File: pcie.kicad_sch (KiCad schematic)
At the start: 21 parts, among them U15 XC7K160T-FFG676

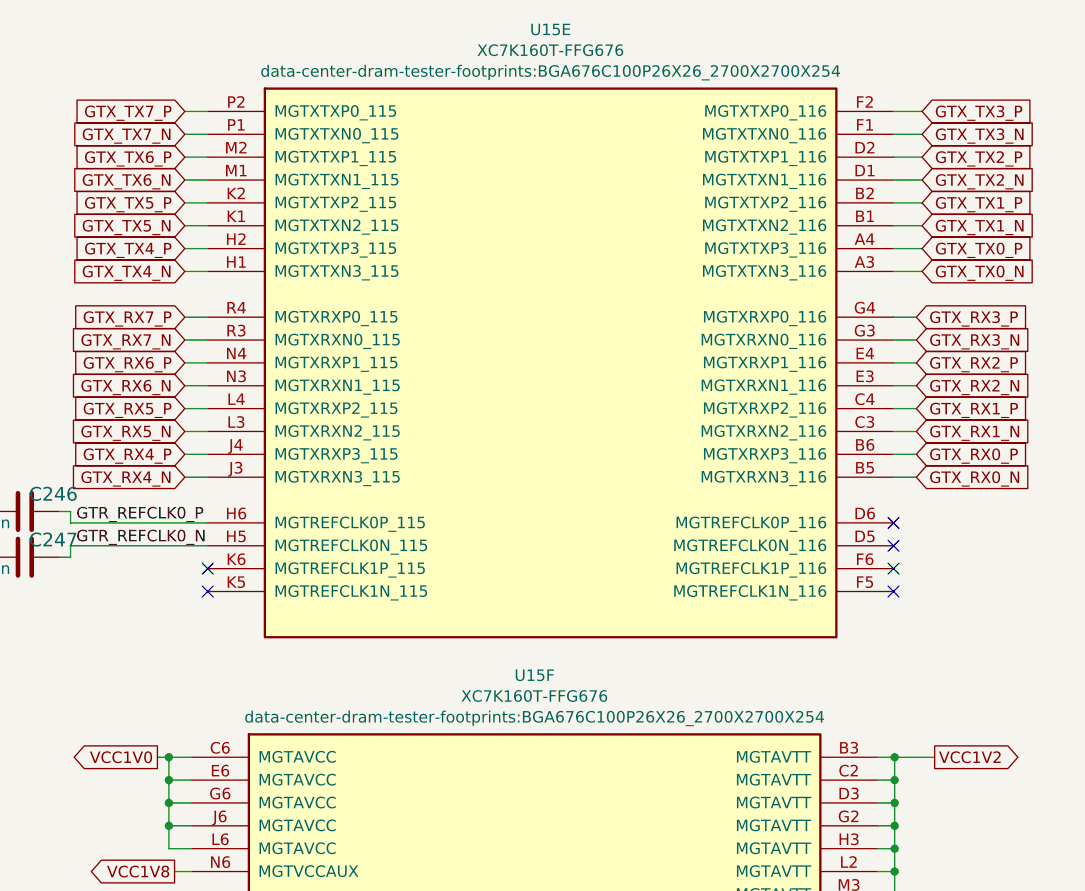
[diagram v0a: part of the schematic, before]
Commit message: Update FPGA symbol (die to pad length), initial fanout for die [1..4]
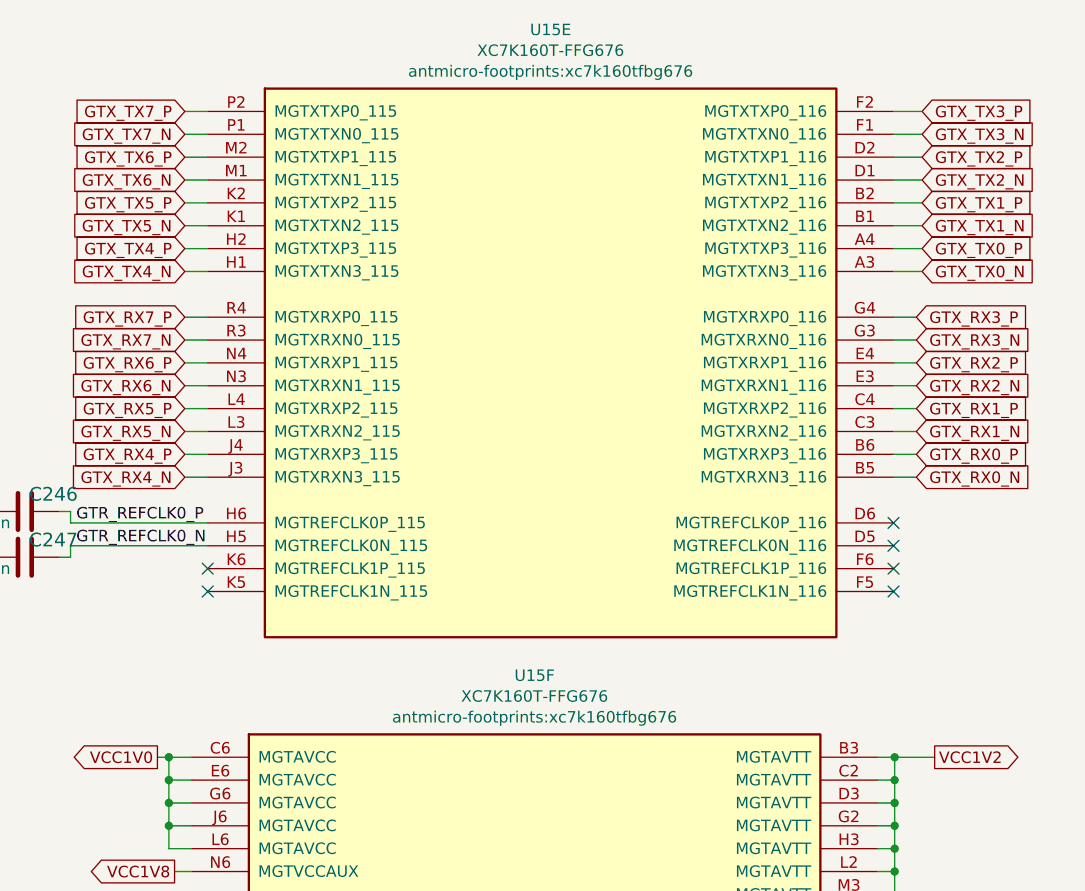
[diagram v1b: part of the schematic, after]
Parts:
- U15: footprint data-center-dram-tester-footprints:BGA676C100P26X26_2700X2700X254 -> antmicro-footprints:xc7k160tfbg676
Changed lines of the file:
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@@
     (property "Reference" "U15" (id 0) (at 155.067 105.8672 0))
     (property "Value" "XC7K160T-FFG676" (id 1) (at 155.067 108.1786 0))
-    (property "Footprint" "data-center-dram-tester-footprints:BGA676C100P26X26_2700X2700X254" (id 2) (at 155.067 110.49 0))
+    (property "Footprint" "antmicro-footprints:xc7k160tfbg676" (id 2) (at 155.067 110.49 0))
     (property "Datasheet" "" (id 3) (at 155.067 127.635 0))
     (pin "AA21")
@@
     (property "Reference" "U15" (id 0) (at 156.845 34.1122 0))
     (property "Value" "XC7K160T-FFG676" (id 1) (at 156.845 36.4236 0))
-    (property "Footprint" "data-center-dram-tester-footprints:BGA676C100P26X26_2700X2700X254" (id 2) (at 156.845 38.735 0))
+    (property "Footprint" "antmicro-footprints:xc7k160tfbg676" (id 2) (at 156.845 38.735 0))
     (property "Datasheet" "" (id 3) (at 156.845 71.12 0))
     (pin "AA21")

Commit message: Cleanup schematic
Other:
- note added: "BANK 115"
- note added: "BANK 116"
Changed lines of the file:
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@@
   (title_block
     (title "Data Center DRAM Tester")
-    (date "2022-09-07")
+    (date "2022-10-31")
     (rev "1.2.0")
     (comment 1 "www.antmicro.com")
@@
   )
   (junction (at 136.525 172.974) (diameter 0) (color 0 0 0 0)
-  )
-  (junction (at 62.992 184.15) (diameter 0) (color 0 0 0 0)
   )
   (junction (at 82.042 184.15) (diameter 0) (color 0 0 0 0)
@@
     (stroke (width 0) (type default) (color 0 0 0 0))
   )
-  (wire (pts (xy 56.515 184.15) (xy 62.992 184.15))
-    (stroke (width 0) (type default) (color 0 0 0 0))
-  )
   (wire (pts (xy 194.945 81.28) (xy 197.485 81.28))
     (stroke (width 0) (type default) (color 0 0 0 0))
@@
     (stroke (width 0) (type default) (color 0 0 0 0))
   )
+  (text "BANK 115" (at 104.14 34.29 0)
+    (effects (font (size 2.4892 2.4892) (thickness 0.4978) bold) (justify left bottom))
+  )
+  (text "BANK 116" (at 189.23 34.29 0)
+    (effects (font (size 2.4892 2.4892) (thickness 0.4978) bold) (justify left bottom))
+  )
   (text "Trace length from the resistor pins to the\nFPGA pins MGTRREF and MGTAVTTRCAL\nmust be equal in length."

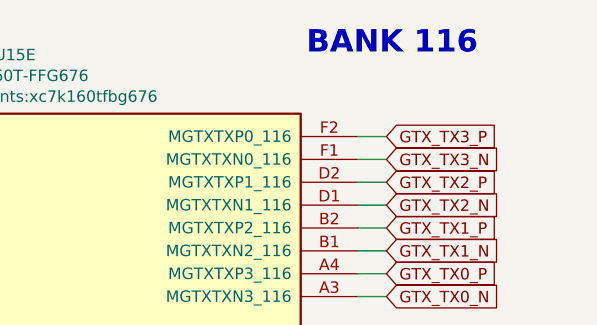
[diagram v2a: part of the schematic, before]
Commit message: Replace visualisation in README and schematic
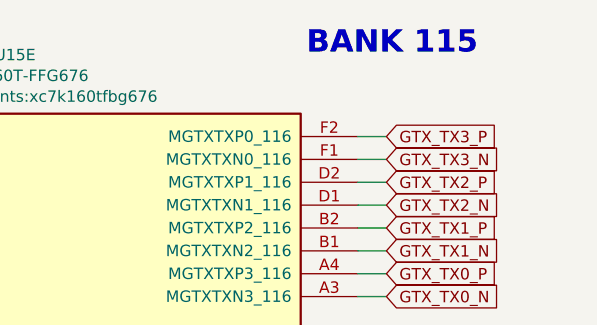
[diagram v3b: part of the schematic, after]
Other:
- note removed: "BANK 116"
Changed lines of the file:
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@@
     (effects (font (size 2.4892 2.4892) (thickness 0.4978) bold) (justify left bottom))
   )
-  (text "BANK 116" (at 189.23 34.29 0)
+  (text "BANK 115" (at 189.23 34.29 0)
     (effects (font (size 2.4892 2.4892) (thickness 0.4978) bold) (justify left bottom))
   )

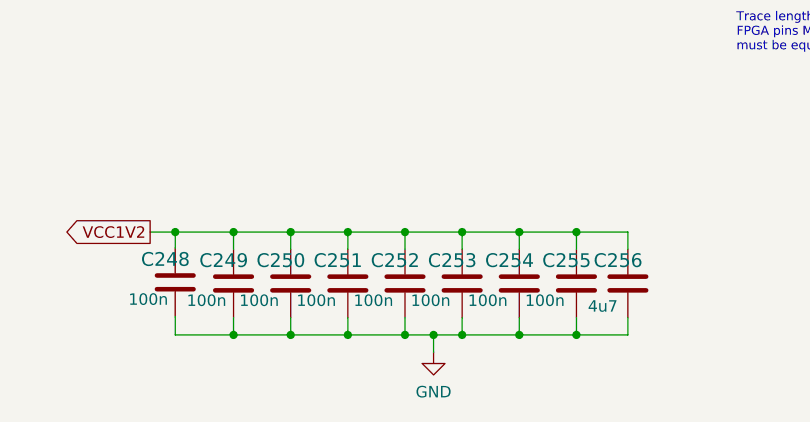
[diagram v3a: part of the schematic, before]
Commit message: Assign and connect misc. signals. Add, place and route decoupling capacitors
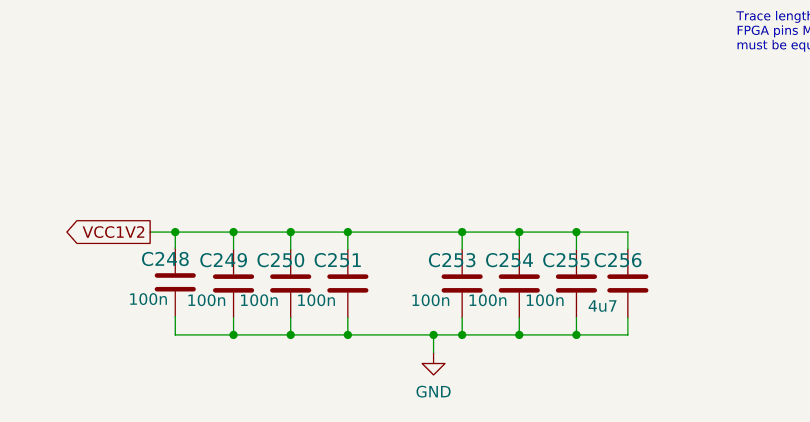
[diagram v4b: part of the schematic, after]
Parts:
- removed C252: C_100n_0201, antmicro-footprints:0201-res, symbol antmicroCapacitorsmisc:C_100n_0201
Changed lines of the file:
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@@
   (junction (at 146.05 184.404) (diameter 0) (color 0 0 0 0)
   )
-  (junction (at 142.875 184.404) (diameter 0) (color 0 0 0 0)
-  )
   (junction (at 130.175 172.974) (diameter 0) (color 0 0 0 0)
   )
@@
   )
   (junction (at 195.072 114.935) (diameter 0) (color 0 0 0 0)
-  )
-  (junction (at 142.875 172.974) (diameter 0) (color 0 0 0 0)
   )
   (junction (at 75.692 184.15) (diameter 0) (color 0 0 0 0)
@@
     (stroke (width 0) (type default) (color 0 0 0 0))
   )
-  (wire (pts (xy 142.875 172.974) (xy 149.225 172.974))
+  (wire (pts (xy 136.525 172.974) (xy 149.225 172.974))
     (stroke (width 0) (type default) (color 0 0 0 0))
   )
@@
     (stroke (width 0) (type default) (color 0 0 0 0))
   )
-  (wire (pts (xy 142.875 184.404) (xy 136.525 184.404))
+  (wire (pts (xy 136.525 184.404) (xy 146.05 184.404))
     (stroke (width 0) (type default) (color 0 0 0 0))
   )
@@
     (stroke (width 0) (type default) (color 0 0 0 0))
   )
-  (wire (pts (xy 136.525 172.974) (xy 142.875 172.974))
-    (stroke (width 0) (type default) (color 0 0 0 0))
-  )
   (wire (pts (xy 87.63 88.9) (xy 90.17 88.9))
     (stroke (width 0) (type default) (color 0 0 0 0))
@@
     (stroke (width 0) (type default) (color 0 0 0 0))
   )
-  (wire (pts (xy 142.875 184.404) (xy 146.05 184.404))
-    (stroke (width 0) (type default) (color 0 0 0 0))
-  )
   (wire (pts (xy 62.992 172.72) (xy 62.992 174.625))
     (stroke (width 0) (type default) (color 0 0 0 0))
@@
     (stroke (width 0) (type default) (color 0 0 0 0))
   )
-  (wire (pts (xy 142.875 182.499) (xy 142.875 184.404))
-    (stroke (width 0) (type default) (color 0 0 0 0))
-  )
   (wire (pts (xy 116.205 76.2) (xy 118.745 76.2))
     (stroke (width 0) (type default) (color 0 0 0 0))
@@
   )
   (wire (pts (xy 116.205 45.72) (xy 118.745 45.72))
-    (stroke (width 0) (type default) (color 0 0 0 0))
-  )
-  (wire (pts (xy 142.875 172.974) (xy 142.875 174.879))
     (stroke (width 0) (type default) (color 0 0 0 0))
   )
@@
     (pin "1")
     (pin "2")
-  )
-  (symbol (lib_id "antmicroCapacitorsmisc:C_100n_0201") (at 142.875 178.689 0) (unit 1)
-    (in_bom yes) (on_board yes)
-    (property "Reference" "C252" (id 0) (at 139.065 176.149 0)
-      (effects (font (size 1.524 1.524)) (justify left))
-    )
-    (property "Value" "C_100n_0201" (id 1) (at 142.875 182.499 0)
-      (effects (font (size 1.524 1.524)) hide)
-    )
-    (property "Footprint" "antmicro-footprints:0201-res" (id 2) (at 147.955 173.609 0)
-      (effects (font (size 1.524 1.524)) (justify left) hide)
-    )
-    (property "Datasheet" "" (id 3) (at 142.875 178.689 0)
-      (effects (font (size 1.27 1.27)) hide)
-    )
-    (property "Manufacturer" "YAGEO" (id 4) (at 147.955 168.529 0)
-      (effects (font (size 1.524 1.524)) (justify left) hide)
-    )
-    (property "MPN" "CC0201KRX6S5BB104" (id 5) (at 147.955 171.069 0)
-      (effects (font (size 1.524 1.524)) (justify left) hide)
-    )
-    (property "Val" "100n" (id 6) (at 137.16 180.594 0)
-      (effects (font (size 1.27 1.27)) (justify left))
-    )
-    (pin "1")
-    (pin "2")

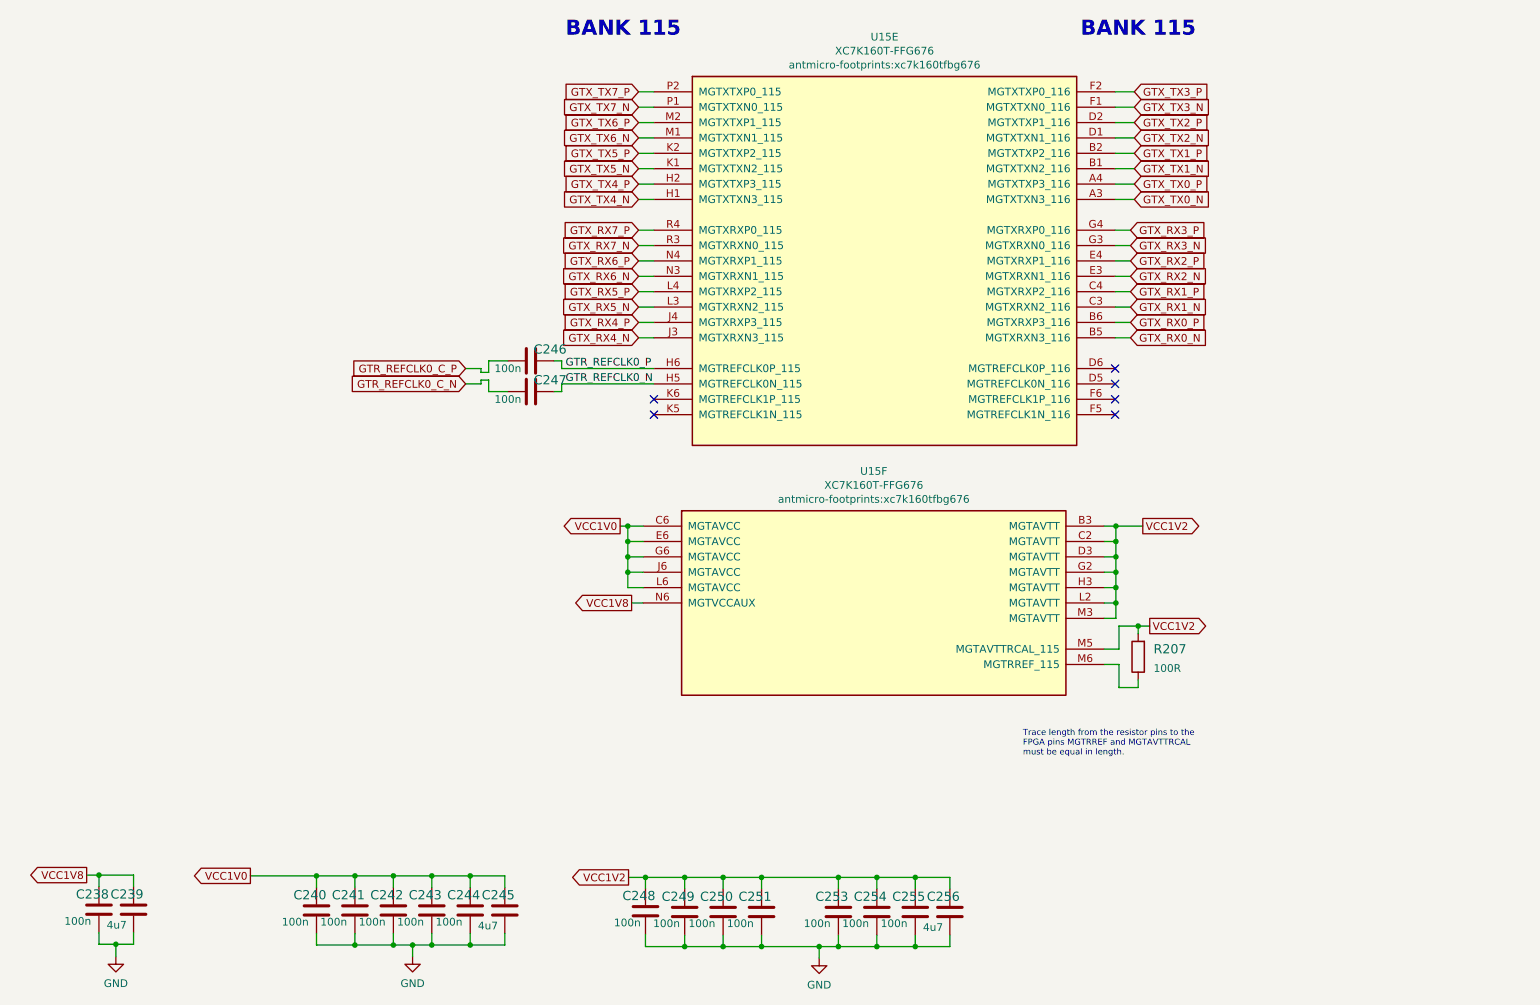
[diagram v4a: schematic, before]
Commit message: Draw power supply polygons
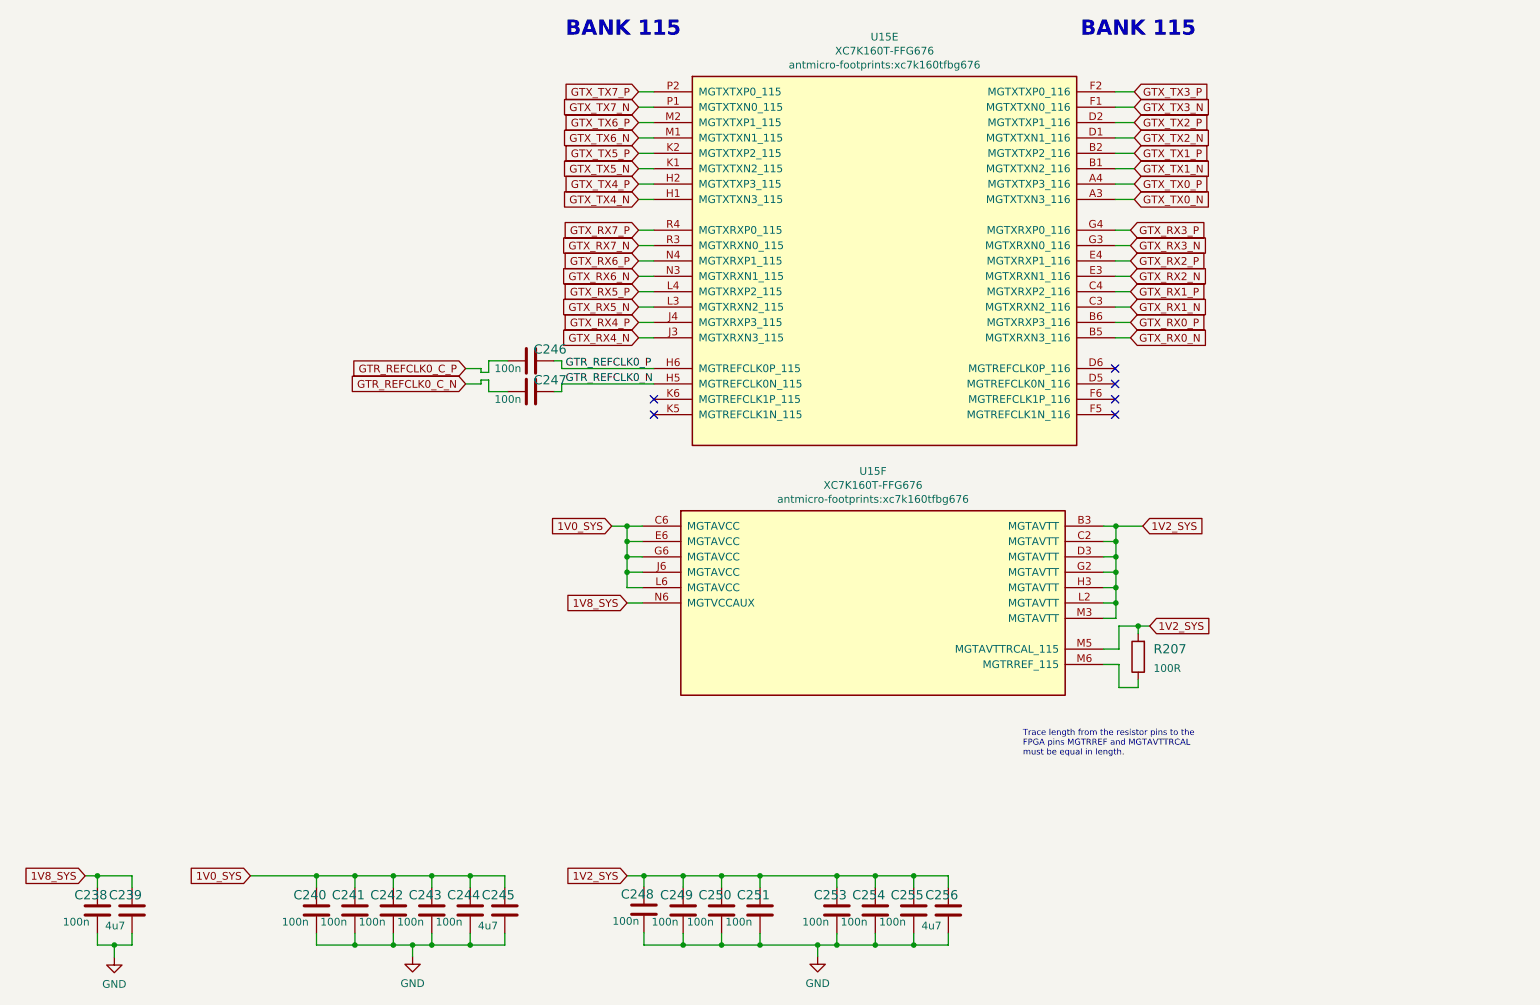
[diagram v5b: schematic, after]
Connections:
- net VCC1V0 renamed 1V0_SYS
- net VCC1V2 renamed 1V2_SYS
- net VCC1V8 renamed 1V8_SYS

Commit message: Readability improvements
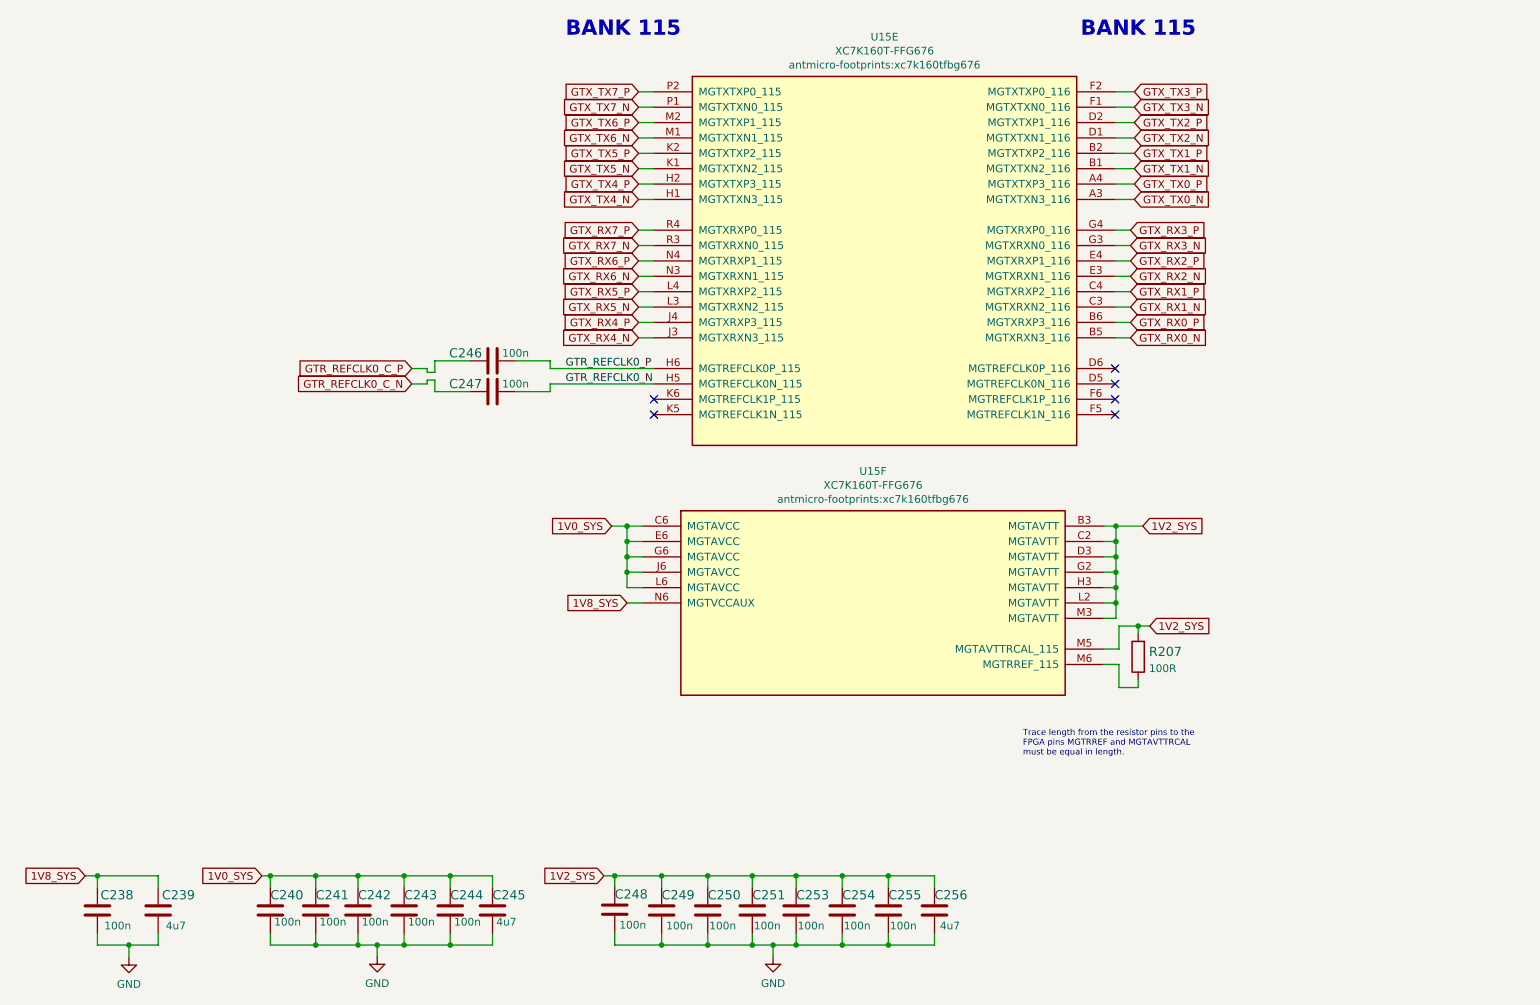
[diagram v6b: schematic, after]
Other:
- moved on the sheet: C239, C240, C241, C242, C243, C244, C245, C246, C247, C248, C249, C250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

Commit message: Final touches
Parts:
- added C314: C_100n_0402, antmicro-footprints:0402-cap, symbol antmicroCapacitors0402:C_100n_0402
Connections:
- net 1V2_SYS: now also C314.1
- net GND: now also C314.2
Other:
- moved on the sheet: C248, C249, C250, C251, C253, C254, C255, C256
